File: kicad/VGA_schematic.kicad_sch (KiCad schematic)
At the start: 4 parts, among them J2 DE15_Pins_HighDensity, U4 74HCT08, U5 74HC74, Y2 20MHz Crystal

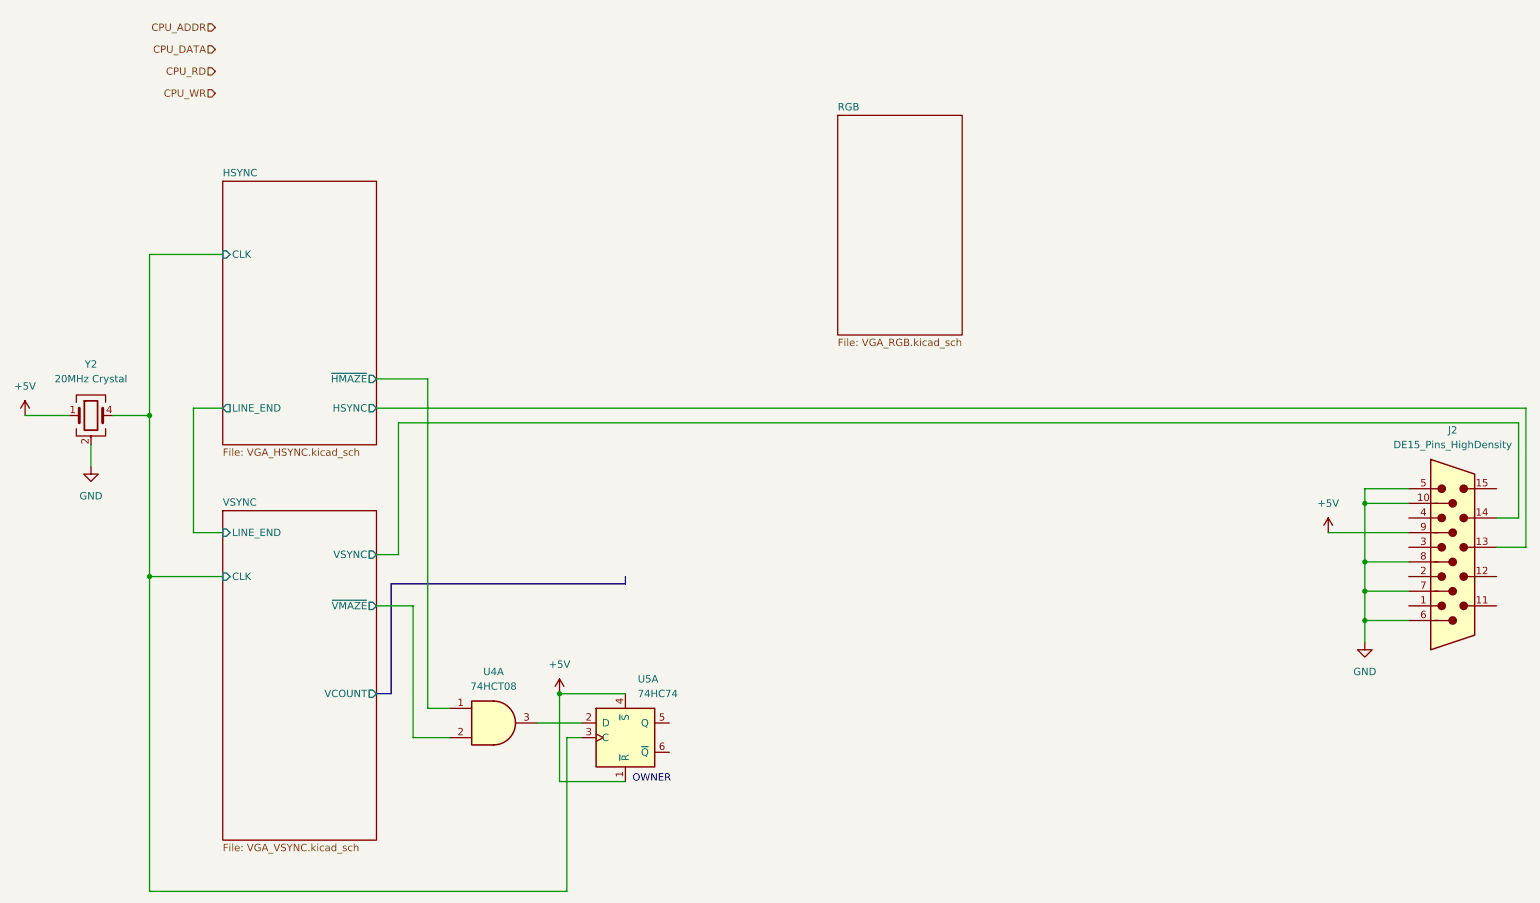
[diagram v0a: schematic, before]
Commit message: Add VRAM address multiplexer to finish off RGB schematic
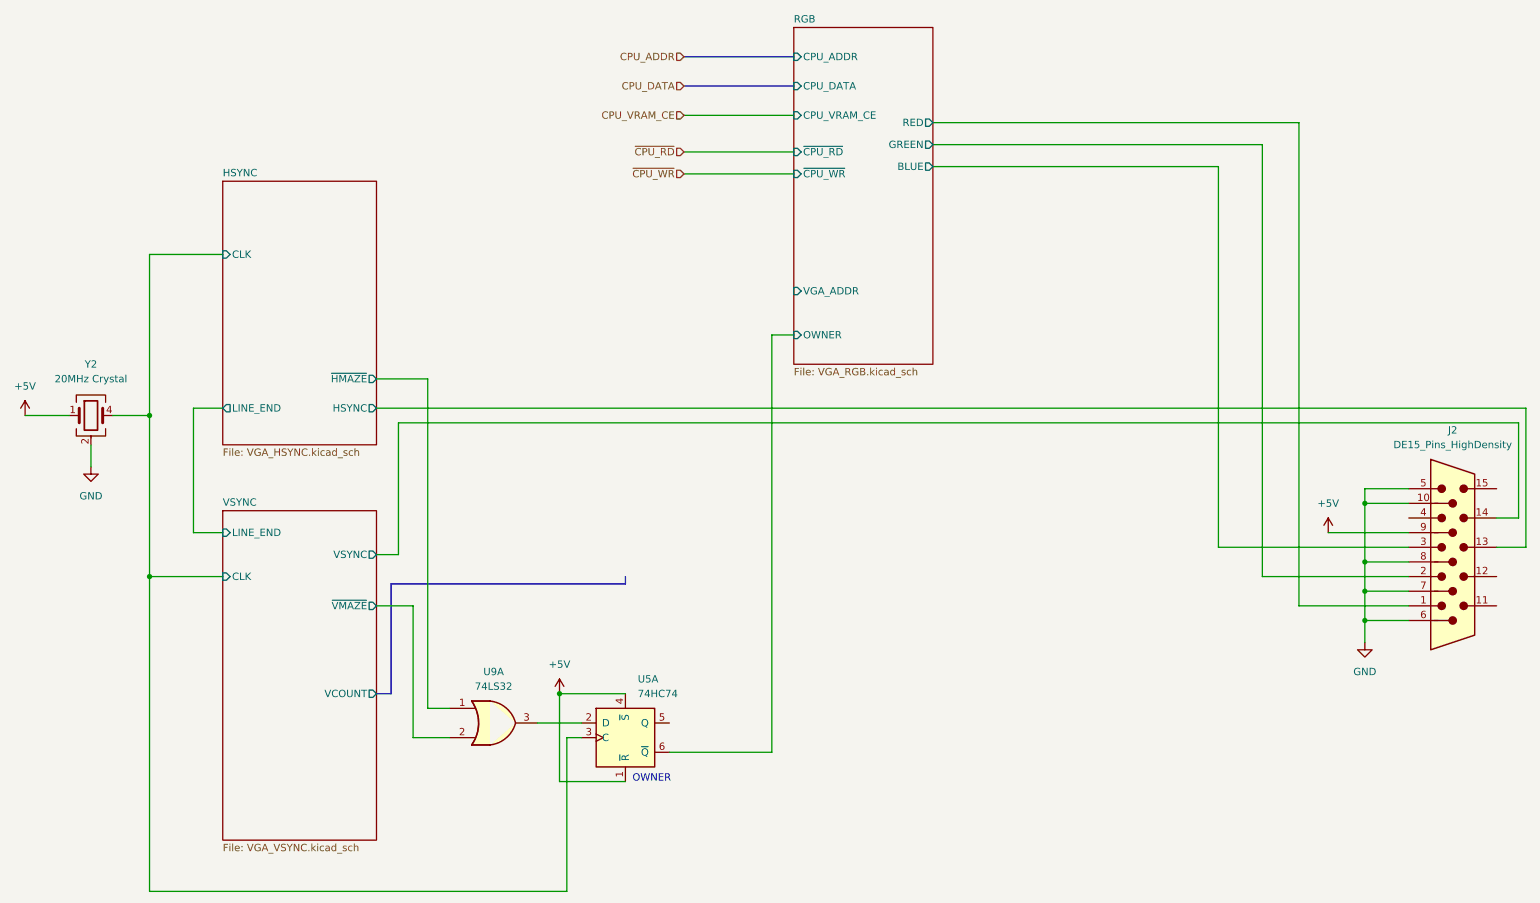
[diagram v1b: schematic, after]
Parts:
- removed U4: 74HCT08, symbol 74xx:74LS08
- added U9: 74LS32, symbol 74xx:74LS32
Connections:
- net HSYNC/~{HMAZE}: now also U9.1
- net VSYNC/~{VMAZE}: now also U9.2
- net at U5.2 (D): now also U9.3
- net RGB/OWNER: now reaches U5.6 (~{Q})
- net RGB/RED: now reaches J2.1
- net RGB/GREEN: now reaches J2.2
- net RGB/BLUE: now reaches J2.3
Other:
- sheet RGB ports: added BLUE, CPU_ADDR, CPU_DATA, CPU_VRAM_CE, GREEN, OWNER, RED, VGA_ADDR, ~{CPU_RD}, ~{CPU_WR}; removed none
